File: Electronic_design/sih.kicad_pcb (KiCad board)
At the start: 2 copper layers, 20 parts, among them U1 ESP32-D0WD, U2 AP2112K-3.3, U3 TP4057, U4 LM358, Y1 40MHz

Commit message: PCB design and schematic modified
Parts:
- BT1: footprint Battery:BatteryHolder_Keystone_103_1x20mm -> Battery:BatteryHolder_Keystone_2998_1x6.8mm
- RV1: value R_Potentiometer -> 10 K
- U3: footprint Package_SO:SOIC-8-1EP_3.9x4.9mm_P1.27mm_EP2.29x3mm -> Package_TO_SOT_SMD:SOT-23-6
- U4: footprint Package_DIP:DIP-8-16_W7.62mm -> Package_SO:SOIC-8-1EP_3.9x4.9mm_P1.27mm_EP2.29x3mm
- moved RV1 102.6 mm to (57.5, 75.0)
- moved U1 64.7 mm to (101.3, 76.5)
- moved U2 62.5 mm to (84.0, 75.0)
- moved U3 61.3 mm to (93.0, 76.5)
- moved BT1 52.7 mm to (71.5, 76.0)
- moved C4 43.2 mm to (108.3, 75.0)
- moved C5 43.2 mm to (108.3, 77.5)
- moved R2 43.2 mm to (112.3, 75.0)
- moved R3 43.2 mm to (112.3, 77.5)
- moved C2 35.8 mm to (117.8, 76.0)
- moved C3 35.8 mm to (117.8, 78.5)
- moved C7 35.8 mm to (121.8, 76.0)
- moved R1 35.8 mm to (121.8, 78.5)
- moved R5 35.8 mm to (125.8, 76.0)
- moved Y1 35.8 mm to (125.8, 78.5)
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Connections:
- C7 pad 2: GND -> Net-(U4A-+)
- R2 pad 2: 3.3V -> Net-(U2-VOUT)
- R3 pad 1: 3.3V -> Net-(U2-VOUT)
- R3 pad 2: GND -> Net-(U4A-+)
- R4 pad 2: GND -> Net-(U4A-+)
- RV1 pad 2: GND -> Net-(U4A-+)
- U4 pad 3: GND -> Net-(U4A-+)

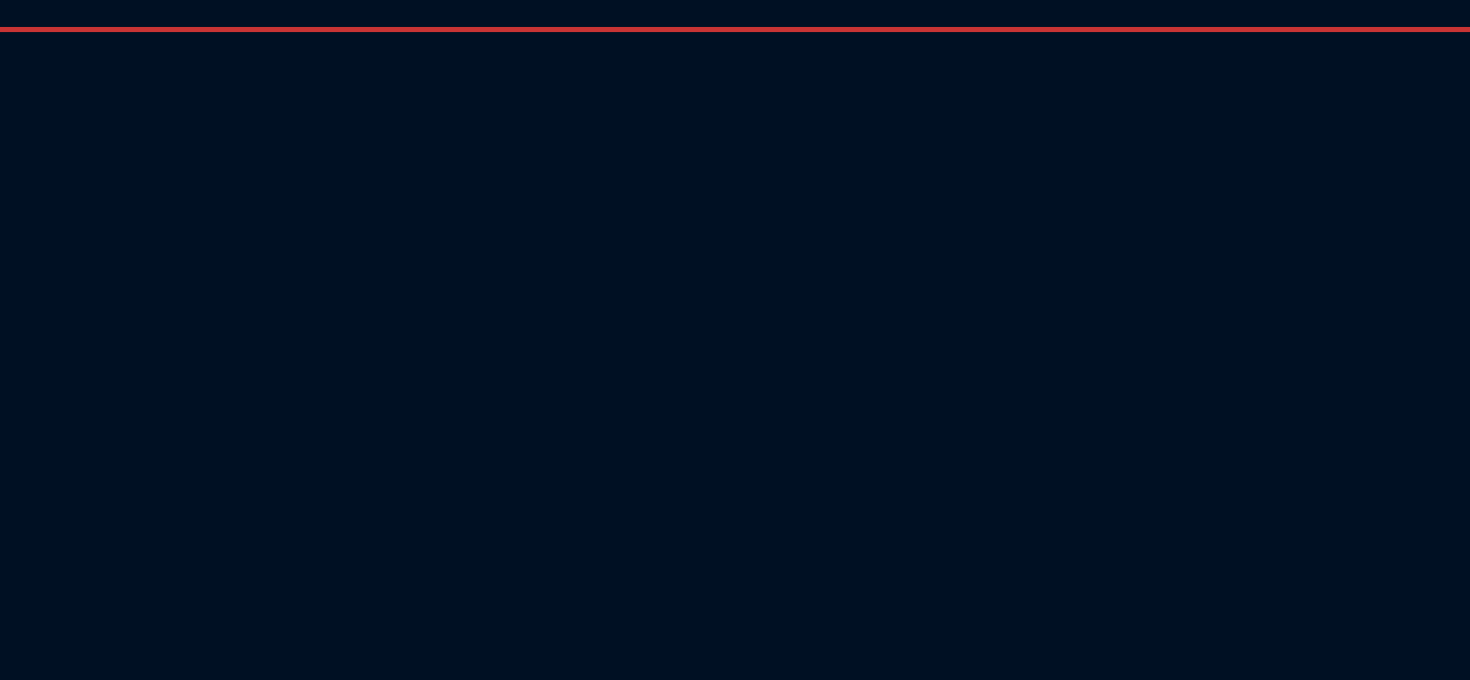
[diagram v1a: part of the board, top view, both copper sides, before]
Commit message: Updated design with all components
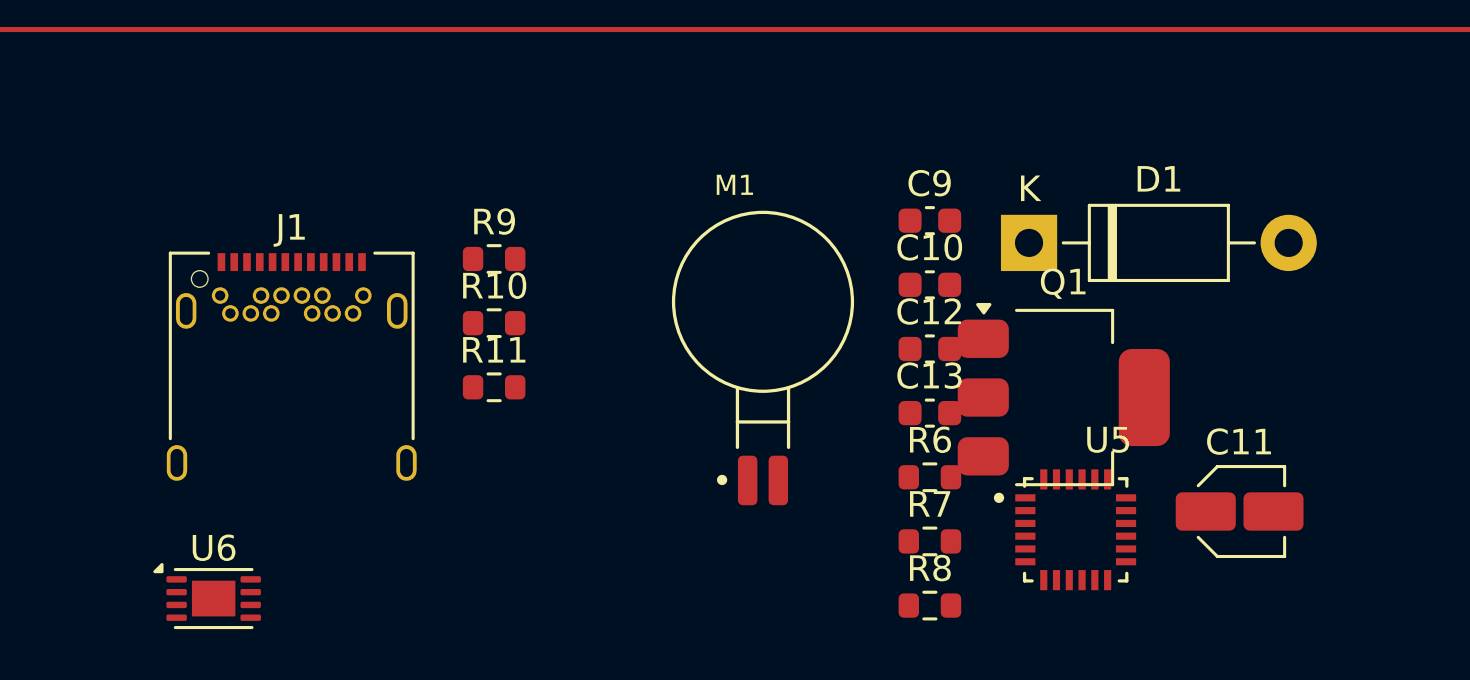
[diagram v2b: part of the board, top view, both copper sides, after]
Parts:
- added C10: 0.1u, Capacitor_SMD:C_0603_1608Metric, F.Cu at (112.2, 93.0)
- added C11: C_Polarized, Capacitor_SMD:C_Elec_3x5.4, F.Cu at (124.3, 101.9)
- added C12: 100n, Capacitor_SMD:C_0603_1608Metric, F.Cu at (112.2, 95.5)
- added C13: 10u, Capacitor_SMD:C_0603_1608Metric, F.Cu at (112.2, 98.0)
- added C9: 10u, Capacitor_SMD:C_0603_1608Metric, F.Cu at (112.2, 90.5)
- added D1: 1N5819, Diode_THT:D_DO-41_SOD81_P10.16mm_Horizontal, F.Cu at (116.1, 91.3)
- added J1: USB_C_Receptacle_PowerOnly_6P, Connector_USB:USB_C_Receptacle_Amphenol_12401548E4-2A, F.Cu at (87.3, 97.1)
- added M1: C0720B001F, C0720B001F:XDCR_C0720B001F, F.Cu at (105.7, 95.6)
- added Q1: IRLZ44N, Package_TO_SOT_SMD:SOT-223, F.Cu at (117.5, 97.4)
- added R10: 5.1k, Resistor_SMD:R_0603_1608Metric, F.Cu at (95.2, 94.5)
- added R11: R_prog, Resistor_SMD:R_0603_1608Metric, F.Cu at (95.2, 97.0)
- added R6: 4.7k, Resistor_SMD:R_0603_1608Metric, F.Cu at (112.2, 100.5)
- added R7: 4.7k, Resistor_SMD:R_0603_1608Metric, F.Cu at (112.2, 103.0)
- added R8: 10k, Resistor_SMD:R_0603_1608Metric, F.Cu at (112.2, 105.5)
- added R9: 5.1k, Resistor_SMD:R_0603_1608Metric, F.Cu at (95.2, 92.0)
- added U5: MPU-6050, MPU-6050:QFN50P400X400X95-24N, F.Cu at (117.9, 102.6)
- added U6: MCP73831-2-MC, Package_DFN_QFN:DFN-8-1EP_3x2mm_P0.5mm_EP1.7x1.4mm, F.Cu at (84.2, 105.3)
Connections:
- C3 pad 2: Net-(U3-V_{CC}) -> 5v
- R1 pad 1: 5V -> 5v
- U1 pad 24: unconnected-(U1-GPIO4-Pad24) -> Net-(U1-GPIO4)
- U1 pad 25: unconnected-(U1-GPIO16-Pad25) -> Net-(U1-GPIO16)
- U1 pad 39: unconnected-(U1-GPIO22-Pad39) -> Net-(U1-GPIO22)
- U1 pad 42: unconnected-(U1-GPIO21-Pad42) -> Net-(U1-GPIO21)
- U2 pad 1: 5V -> 5v
- U3 pad 4: Net-(U3-V_{CC}) -> 5v
- U3 pad 6: unconnected-(U3-PROG-Pad6) -> Net-(U3-PROG)
